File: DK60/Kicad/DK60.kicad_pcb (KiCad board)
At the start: 2 copper layers, 285.1 x 94.3 mm, 171 parts, among them J1 USB_mini_micro_B, K1 K00, K10 K09, K11 K0A, K12 K0B, K13 K0C, K14 K10, K15 K11, K16 K12, K17 K13, K18 K14, K19 K15, K2 K01, K20 K16, K21 K17, K22 K18, K23 K19, K24 K1A, K25 K1B, K26 K1C, K27 K20, K28 K21, K29 K22, K3 K02, K30 K23, K31 K24, K32 K25, K33 K26, K34 K27, K35 K28, K36 K29, K37 K2A, K38 K2B, K39 K2C, K4 K03, K40 K30, K41 K31, K42 K32, K43 K33, K44 K34, K45 K35, K46 K36, K47 K37, K48 K38, K49 K39, K5 K04, K50 K3A, K51 K3B, K52 K3C, K53 K41, K54 K42, K55 K45, K56 K48, K57 K49, K58 K4A, K59 K4B, K6 K05, K60 K4C, K61 Ctrl, K62 L_ALT, K63 SPACE, K64 SPACE, K65 R_ALT, K66 R_ALT, K67 R_GUI, K68 R_GUI, K69 K30, K7 K06, K70 K3C, K71 K3B, K72 SPACE, K8 K07, K9 K08, SW1 SW_PUSH, U0 ATMEGA32U4, X1 XTAL_GND

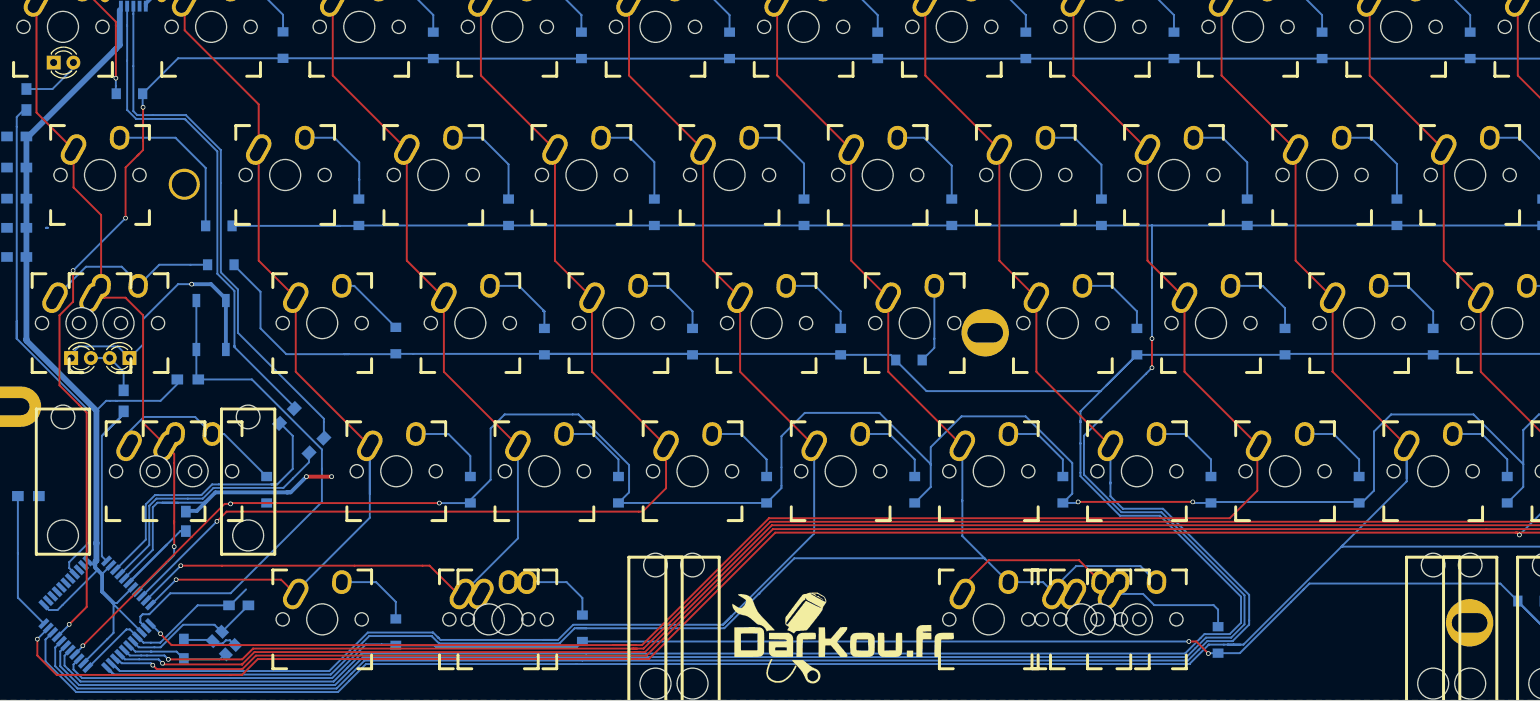
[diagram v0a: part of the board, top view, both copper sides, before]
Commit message: - Updated Led position - Fixed bug for bottom hole - Updated gerber files
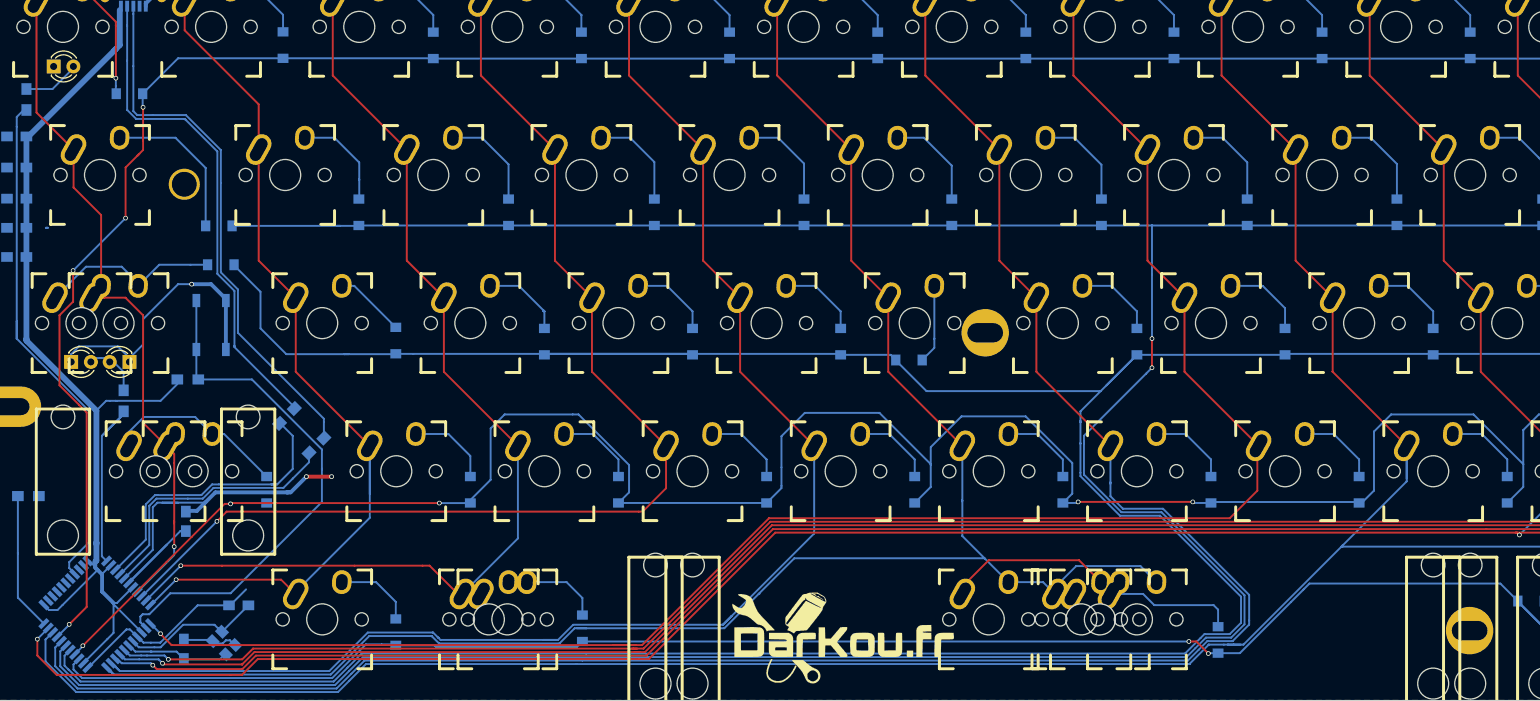
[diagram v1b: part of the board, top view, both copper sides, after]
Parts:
- moved Poker_oval_hole 1.00 mm to (257.1, 184.8)
- moved LD0 0.50 mm to (75.0, 112.2)
- moved LD1 0.50 mm to (77.2, 150.2)
- moved LD2 0.50 mm to (84.8, 150.2)
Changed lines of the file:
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@@
     (links 255)
     (no_connects 0)
-    (area 33.750002 85.500001 374.65 202.9)
+    (area 30.250001 85.500001 374.65 202.9)
     (thickness 1.6)
-    (drawings 23)
+    (drawings 25)
     (tracks 1113)
     (zones 0)
@@
   )
   (module Footprint:Poker_oval_hole (layer F.Cu)
-    (at 257.1 183.8)
+    (at 257.1 184.8)
     (fp_text reference Poker_oval_hole (at 0 0) (layer F.SilkS) hide
       (effects (font (size 1 1) (thickness 0.15)))
@@
   )
   (module LEDs:LED_D3.0mm (layer F.Cu)
-    (at 75 111.75)
+    (at 75 112.25)
     (descr "LED, diameter 3.0mm, 2 pins")
     (tags "LED diameter 3.0mm 2 pins")
@@
   )
   (module LEDs:LED_D3.0mm (layer F.Cu)
-    (at 77.25 149.75)
+    (at 77.25 150.25)
     (descr "LED, diameter 3.0mm, 2 pins")
     (tags "LED diameter 3.0mm 2 pins")
@@
   )
   (module LEDs:LED_D3.0mm (layer F.Cu)
-    (at 84.75 149.75 180)
+    (at 84.75 150.25 180)
     (descr "LED, diameter 3.0mm, 2 pins")
     (tags "LED diameter 3.0mm 2 pins")
@@
       (net 79 /Col5))
   )
+  (dimension 85.3 (width 0.3) (layer Dwgs.User)
+    (gr_text "85.300 mm" (at 36.75 142.15 270) (layer Dwgs.User)
+      (effects (font (size 1.5 1.5) (thickness 0.3)))
+    )
+    (feature1 (pts (xy 66.6 184.8) (xy 35.4 184.8)))
+    (feature2 (pts (xy 66.6 99.5) (xy 35.4 99.5)))
+    (crossbar (pts (xy 38.1 99.5) (xy 38.1 184.8)))
+    (arrow1a (pts (xy 38.1 184.8) (xy 37.513579 183.673496)))
+    (arrow1b (pts (xy 38.1 184.8) (xy 38.686421 183.673496)))
+    (arrow2a (pts (xy 38.1 99.5) (xy 37.513579 100.626504)))
+    (arrow2b (pts (xy 38.1 99.5) (xy 38.686421 100.626504)))
+  )
+  (gr_line (start 257.1 184.8) (end 66.6 184.8) (angle 90) (layer Cmts.User) (width 0.2))
+  (dimension 1 (width 0.3) (layer Cmts.User)
+    (gr_text "1.000 mm" (at 62.250001 99 270) (layer Cmts.User)
+      (effects (font (size 1.5 1.5) (thickness 0.3)))
+    )
+    (feature1 (pts (xy 66.6 99.5) (xy 60.900001 99.5)))
+    (feature2 (pts (xy 66.6 98.5) (xy 60.900001 98.5)))
+    (crossbar (pts (xy 63.600001 98.5) (xy 63.600001 99.5)))
+    (arrow1a (pts (xy 63.600001 99.5) (xy 63.01358 98.373496)))
+    (arrow1b (pts (xy 63.600001 99.5) (xy 64.186422 98.373496)))
+    (arrow2a (pts (xy 63.600001 98.5) (xy 63.01358 99.626504)))
+    (arrow2b (pts (xy 63.600001 98.5) (xy 64.186422 99.626504)))
+  )
   (gr_line (start 257.1 183.8) (end 257.1 184.3) (angle 90) (layer Cmts.User) (width 0.2))
   (dimension 24.9 (width 0.3) (layer Dwgs.User)
@@
     (arrow2b (pts (xy 57.1 99.5) (xy 57.686421 100.626504)))
   )
-  (dimension 85.2 (width 0.3) (layer Dwgs.User)
-    (gr_text "85.200 mm" (at 40.250001 141.2 270) (layer Dwgs.User)
-      (effects (font (size 1.5 1.5) (thickness 0.3)))
-    )
-    (feature1 (pts (xy 66.6 183.8) (xy 38.900001 183.8)))
-    (feature2 (pts (xy 66.6 98.6) (xy 38.900001 98.6)))
-    (crossbar (pts (xy 41.600001 98.6) (xy 41.600001 183.8)))
-    (arrow1a (pts (xy 41.600001 183.8) (xy 41.01358 182.673496)))
-    (arrow1b (pts (xy 41.600001 183.8) (xy 42.186422 182.673496)))
-    (arrow2a (pts (xy 41.600001 98.6) (xy 41.01358 99.726504)))
-    (arrow2b (pts (xy 41.600001 98.6) (xy 42.186422 99.726504)))
-  )
   (dimension 25.2 (width 0.3) (layer Dwgs.User)
